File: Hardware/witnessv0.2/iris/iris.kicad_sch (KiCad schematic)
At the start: 0 parts

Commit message: iris rework
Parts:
- added R33, R34, R35, R36: 0, Resistor_SMD:R_0402_1005Metric, symbol Device:R_Small
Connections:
- new net IO/CANRX: R34.2
- new net IO/CANTX: R33.2
- new net IO/RXD_MCU: R36.2
- new net IO/TXD_MCU: R35.2
- new net MCU/CANRX: R34.1
- new net MCU/CANTX: R33.1
- new net MCU/RXD_MCU: R36.1
- new net MCU/TXD_MCU: R35.1
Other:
- sheet IO ports: added BATT_RAW, CANRX, CANTX, GPIO, RXD_MCU, TXD_MCU; removed none
- sheet MCU ports: added CANRX, CANTX, GPIO, I2C_SCL, I2C_SDA, LSM_CS, LSM_INT1, LSM_INT2, MS56_CS, RAD_BUSY, RAD_CS, RAD_DIO1, RAD_RF_EN, RAD_RST, RXD_MCU, SPI3_CIPO, SPI3_COPI, SPI3_SCLK, TXD_MCU, USB_D+, USB_D-, VSENSE; removed none
- sheet Power ports: added BATT_RAW, VSENSE; removed 5V_EN, 5V_ISENSE, ALL_ISENSE
- sheet Radio ports: added SPI3_CIPO, SPI3_COPI, SPI3_SCLK; removed SPI1_CIPO, SPI1_COPI, SPI1_SCLK
- sheet Sensors ports: added SPI3_CIPO, SPI3_COPI, SPI3_SCLK; removed ICM_CS, ICM_INT1, ICM_INT2, SPI2_CIPO, SPI2_COPI, SPI2_SCLK
- title: (none) -> TOP LEVEL

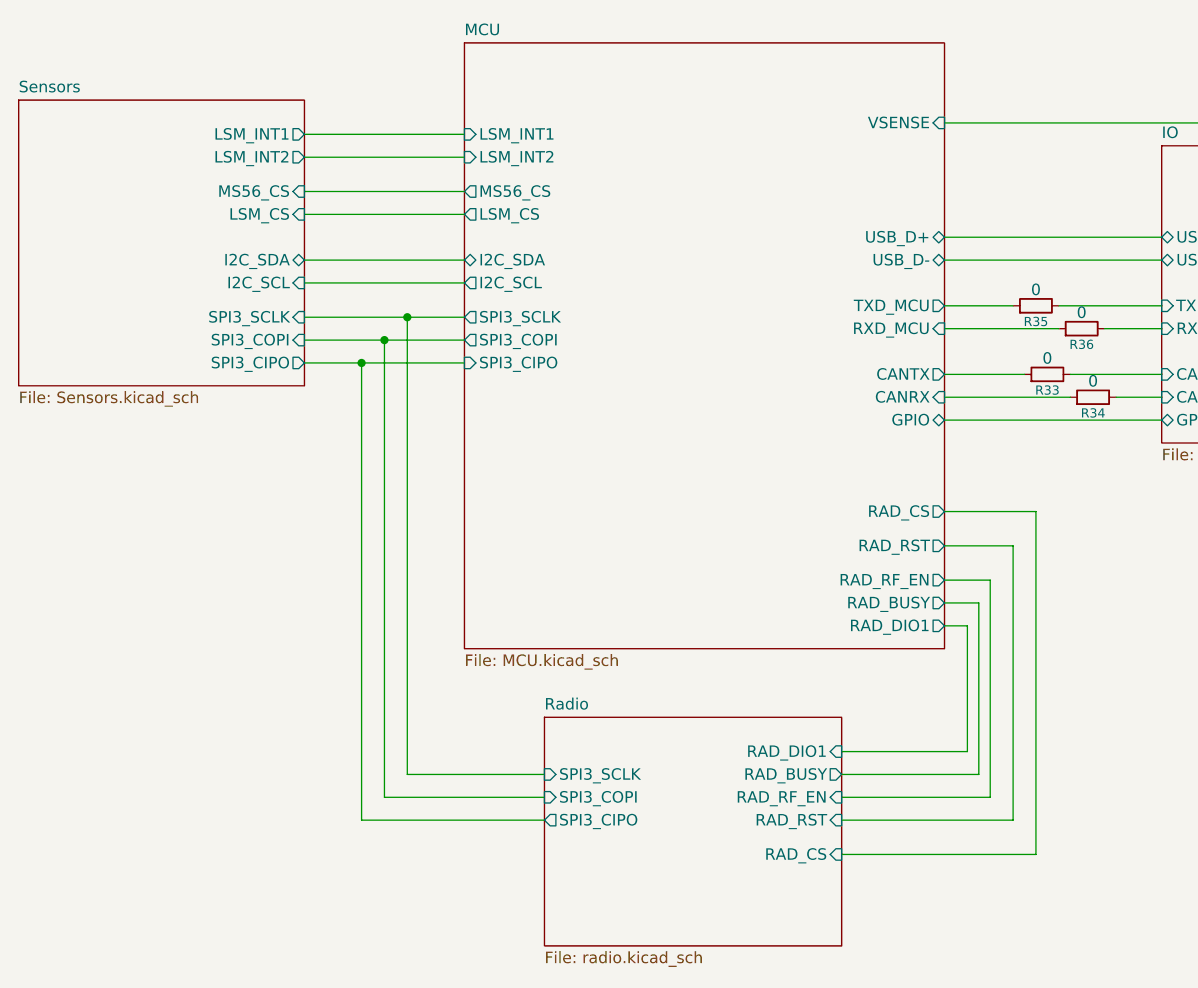
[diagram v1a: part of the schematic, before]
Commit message: trying to make cam board
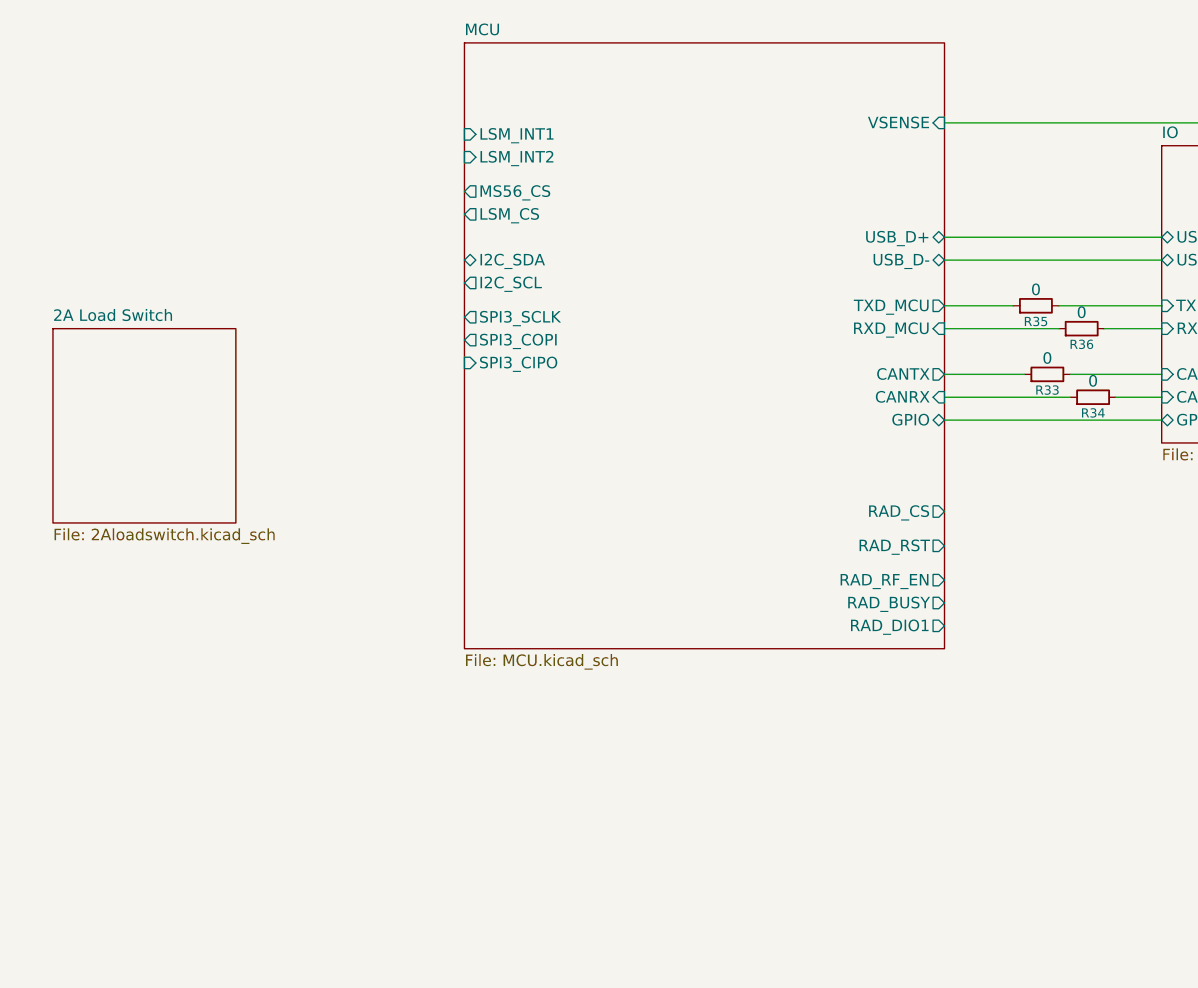
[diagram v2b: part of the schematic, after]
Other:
- removed sheet Radio
- removed sheet Sensors
- added sheet 2A Load Switch (2Aloadswitch.kicad_sch)
